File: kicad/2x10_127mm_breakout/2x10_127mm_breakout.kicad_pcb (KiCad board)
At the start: 2 copper layers, 2 parts

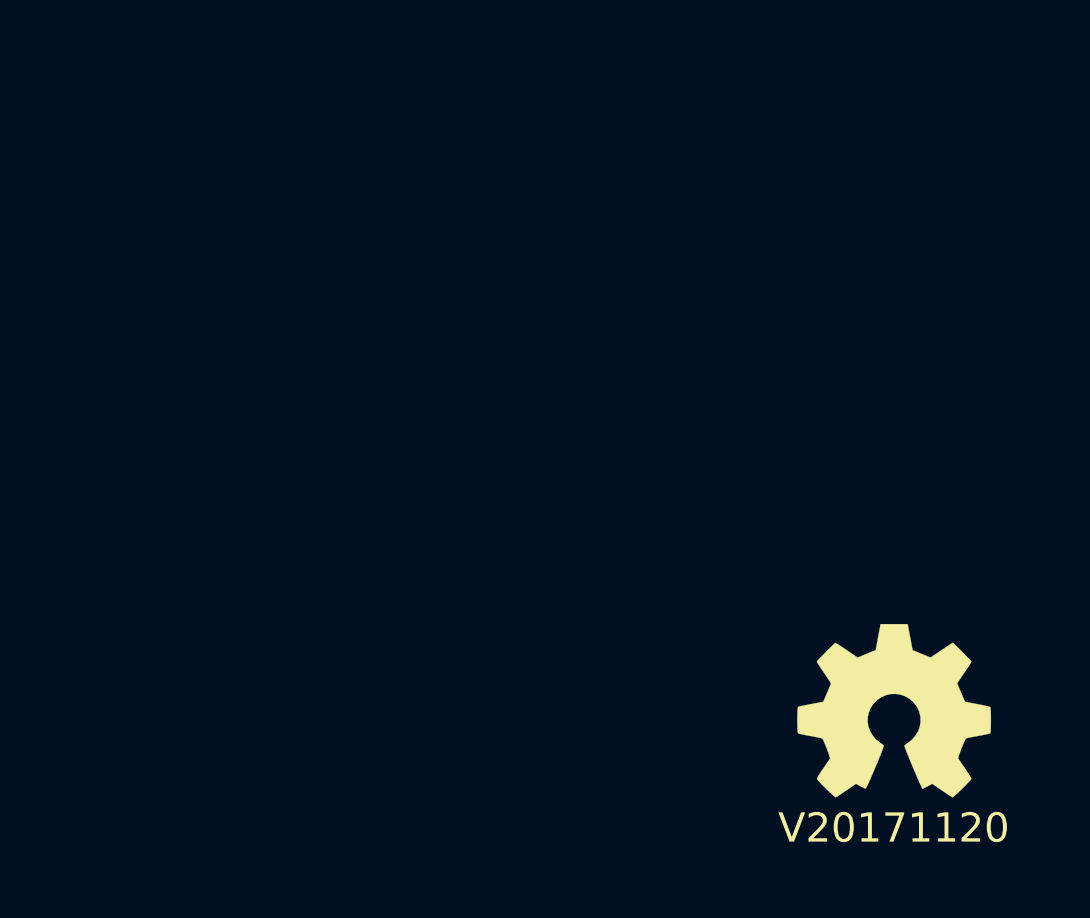
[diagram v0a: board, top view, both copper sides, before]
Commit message: partially layouted 2X10 127mm breakout
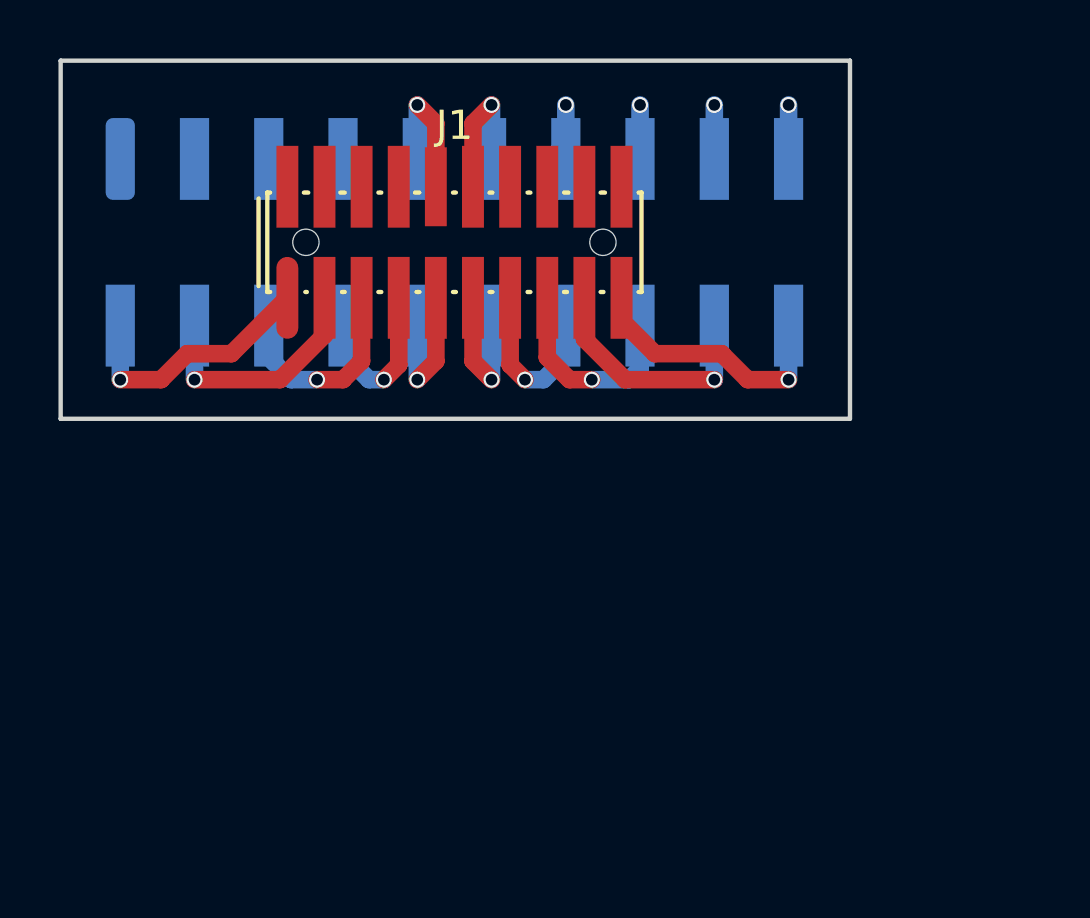
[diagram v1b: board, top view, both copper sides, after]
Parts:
- removed N1: OHWLOGO, Symbols:OSHW-Symbol_6.7x6mm_SilkScreen
- removed N2: V20171120, SquantorLabels:Label_version
- added J1: PINS_2X10, SquantorConnectors:Header-0127-2X10-SMD, F.Cu at (133.0, 85.0)
- added J2: PINS_2X10, SquantorConnectors:Header-0245-2X10-SMD, B.Cu at (133.0, 85.0)
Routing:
- net /pin19: track 0.00 -> 9.17 mm, vias 0 -> 1
- net /pin01: track 0.00 -> 8.72 mm, vias 0 -> 1
- net /pin17: track 0.00 -> 8.27 mm, vias 0 -> 1
- net /pin03: track 0.00 -> 8.20 mm, vias 0 -> 1
- net /pin15: track 0.00 -> 7.15 mm, vias 0 -> 1
- net /pin05: track 0.00 -> 7.00 mm, vias 0 -> 1
- net /pin13: track 0.00 -> 5.81 mm, vias 0 -> 1
- net /pin07: track 0.00 -> 5.73 mm, vias 0 -> 1
- net /pin12: track 0.00 -> 4.91 mm, vias 0 -> 1
- net /pin11: track 0.00 -> 4.91 mm, vias 0 -> 1
- net /pin10: track 0.00 -> 4.91 mm, vias 0 -> 1
- net /pin09: track 0.00 -> 4.91 mm, vias 0 -> 1
- net /pin20: track 0.00 -> 1.85 mm, vias 0 -> 1
- net /pin18: track 0.00 -> 1.85 mm, vias 0 -> 1
- net /pin16: track 0.00 -> 1.85 mm, vias 0 -> 1
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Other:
- board outline added: 27 x 12.2 mm
- rule pad_to_mask_clearance: 0.2 -> 0.1

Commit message: updated PCB and ready for production
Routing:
- net /pin02: track 0.00 -> 9.10 mm, vias 0 -> 1
- net /pin04: track 0.00 -> 8.13 mm, vias 0 -> 1
- net /pin20: track 1.85 -> 9.17 mm
- net /pin06: track 0.00 -> 7.30 mm, vias 0 -> 1
- net /pin18: track 1.85 -> 8.05 mm
- net /pin08: track 0.00 -> 5.96 mm, vias 0 -> 1
- net /pin16: track 1.85 -> 7.08 mm
- net /pin14: track 1.85 -> 5.81 mm
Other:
- board size 27 x 12.2 mm -> 26.9 x 11.3 mm
